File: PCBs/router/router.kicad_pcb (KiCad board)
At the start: 2 copper layers, 77.9 x 90 mm, 0 parts

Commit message: starting to place things
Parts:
- added C1: CP1, Capacitor_THT:CP_Radial_D5.0mm_P2.00mm, F.Cu at (197.1, 58.4)
- added C2: CP1, Capacitor_THT:CP_Radial_D5.0mm_P2.00mm, F.Cu at (202.2, 70.6)
- added C3: C_Small, Capacitor_THT:C_Disc_D5.0mm_W2.5mm_P5.00mm, F.Cu at (133.5, 102.1)
- added C4: C_Small, Capacitor_THT:C_Disc_D5.0mm_W2.5mm_P5.00mm, F.Cu at (133.6, 121.4)
- added C5: C_Small, Capacitor_THT:C_Disc_D4.3mm_W1.9mm_P5.00mm, F.Cu at (148.8, 78.2)
- added C6: C_Small, Capacitor_THT:C_Disc_D5.0mm_W2.5mm_P5.00mm, F.Cu at (157.4, 121.4)
- added C7: C_Small, Capacitor_THT:C_Disc_D5.0mm_W2.5mm_P5.00mm, F.Cu at (157.5, 102.1)
- added C8: C_Small, Capacitor_THT:C_Disc_D4.3mm_W1.9mm_P5.00mm, F.Cu at (172.7, 78.2)
- added D1: LED, LED_THT:LED_D3.0mm, F.Cu at (206.8, 64.5)
- added J1: Conn_01x06_Male, Connector_PinHeader_2.54mm:PinHeader_1x06_P2.54mm_Vertical, F.Cu at (227.6, 88.5)
- added J10: Conn_01x06_Male, Connector_PinHeader_2.54mm:PinHeader_1x06_P2.54mm_Vertical, F.Cu at (148.3, 81.8)
- added J11: Conn_01x06_Male, Connector_PinHeader_2.54mm:PinHeader_1x06_P2.54mm_Vertical, F.Cu at (248.3, 105.8)
- added J12: Conn_01x06_Female, Connector_PinSocket_2.54mm:PinSocket_1x06_P2.54mm_Horizontal, F.Cu at (261.7, 105.8)
- added J13: Conn_01x06_Male, Connector_PinHeader_2.54mm:PinHeader_1x06_P2.54mm_Vertical, F.Cu at (262.2, 88.5)
- added J14: Conn_01x06_Female, Connector_PinSocket_2.54mm:PinSocket_1x06_P2.54mm_Horizontal, F.Cu at (289.0, 88.5)
- added J15: Conn_01x06_Male, Connector_PinHeader_2.54mm:PinHeader_1x06_P2.54mm_Vertical, F.Cu at (172.2, 81.8)
- added J2: Conn_01x06_Male, Connector_PinHeader_2.54mm:PinHeader_1x06_P2.54mm_Horizontal, F.Cu at (230.2, 123.2)
- added J3: Conn_01x06_Male, Connector_PinHeader_2.54mm:PinHeader_1x06_P2.54mm_Vertical, F.Cu at (243.6, 105.8)
- added J4: Conn_01x06_Male, Connector_PinHeader_2.54mm:PinHeader_1x06_P2.54mm_Horizontal, F.Cu at (230.2, 105.8)
- added J5: Conn_01x06_Male, Connector_PinHeader_2.54mm:PinHeader_1x06_P2.54mm_Vertical, F.Cu at (252.9, 88.5)
- added J6: Conn_01x06_Male, Connector_PinHeader_2.54mm:PinHeader_1x06_P2.54mm_Horizontal, F.Cu at (239.5, 88.5)
- added J7: Conn_01x04_Male, Connector_PinHeader_2.54mm:PinHeader_1x04_P2.54mm_Vertical, F.Cu at (222.8, 125.8)
- added J8: Conn_01x06_Male, Connector_PinHeader_2.54mm:PinHeader_1x06_P2.54mm_Vertical, F.Cu at (234.9, 88.5)
- added J9: Conn_01x06_Female, Connector_PinSocket_2.54mm:PinSocket_1x06_P2.54mm_Horizontal, F.Cu at (275.6, 88.5)
- added R1: R, Resistor_THT:R_Axial_DIN0207_L6.3mm_D2.5mm_P7.62mm_Horizontal, F.Cu at (134.1, 85.9)
- added R2: R, Resistor_THT:R_Axial_DIN0207_L6.3mm_D2.5mm_P7.62mm_Horizontal, F.Cu at (210.3, 59.4)
- added R3: R, Resistor_THT:R_Axial_DIN0207_L6.3mm_D2.5mm_P7.62mm_Horizontal, F.Cu at (158.0, 85.9)
- added SW1: SW_MEC_5E, Button_Switch_THT:SW_TH_Tactile_Omron_B3F-10xx, F.Cu at (137.2, 81.3)
- added SW2: SW_MEC_5E, Button_Switch_THT:SW_TH_Tactile_Omron_B3F-10xx, F.Cu at (161.0, 81.3)
- added U1: LM7805_TO220, Package_TO_SOT_THT:TO-220-3_Vertical, F.Cu at (197.1, 65.5)
- added U2: ATmega328P-PU, Package_DIP:DIP-28_W7.62mm_Socket, F.Cu at (136.7, 88.9)
- added U3: ATmega328P-PU, Package_DIP:DIP-28_W7.62mm_Socket, F.Cu at (160.5, 88.9)
- added Y1: Crystal, SamacSys_Parts:HC_49US__AT49_PTH, F.Cu at (130.6, 111.8)
- added Y2: Crystal, SamacSys_Parts:HC_49US__AT49_PTH, F.Cu at (154.4, 111.8)

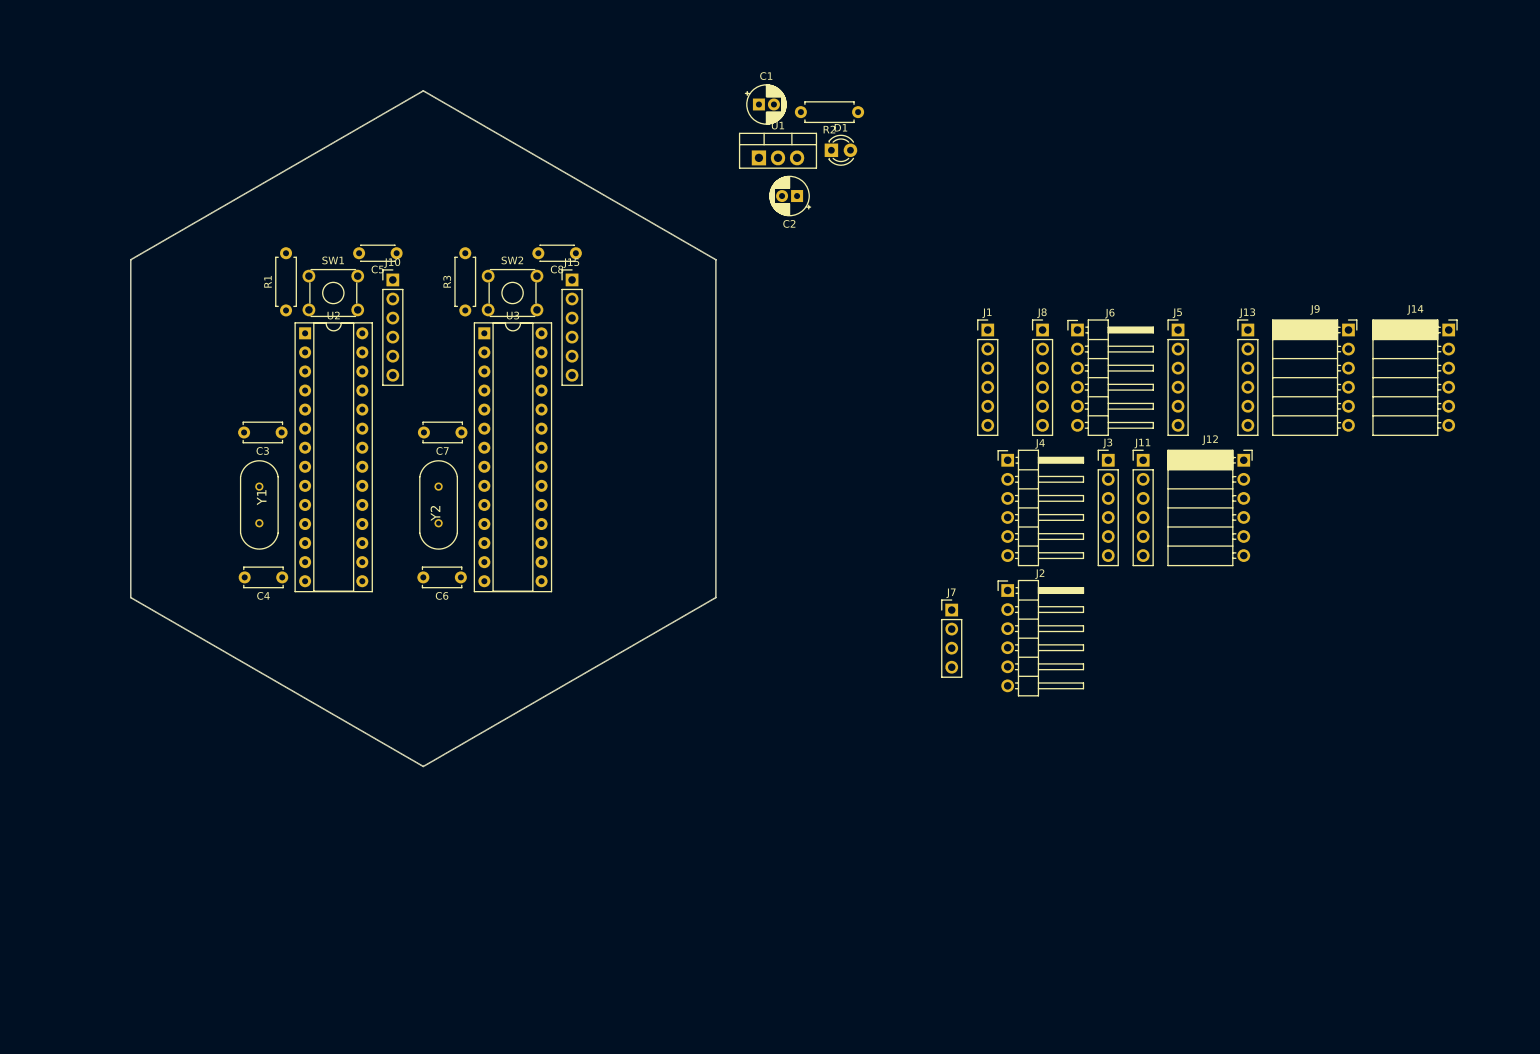
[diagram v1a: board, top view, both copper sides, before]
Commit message: add edges and update footprints
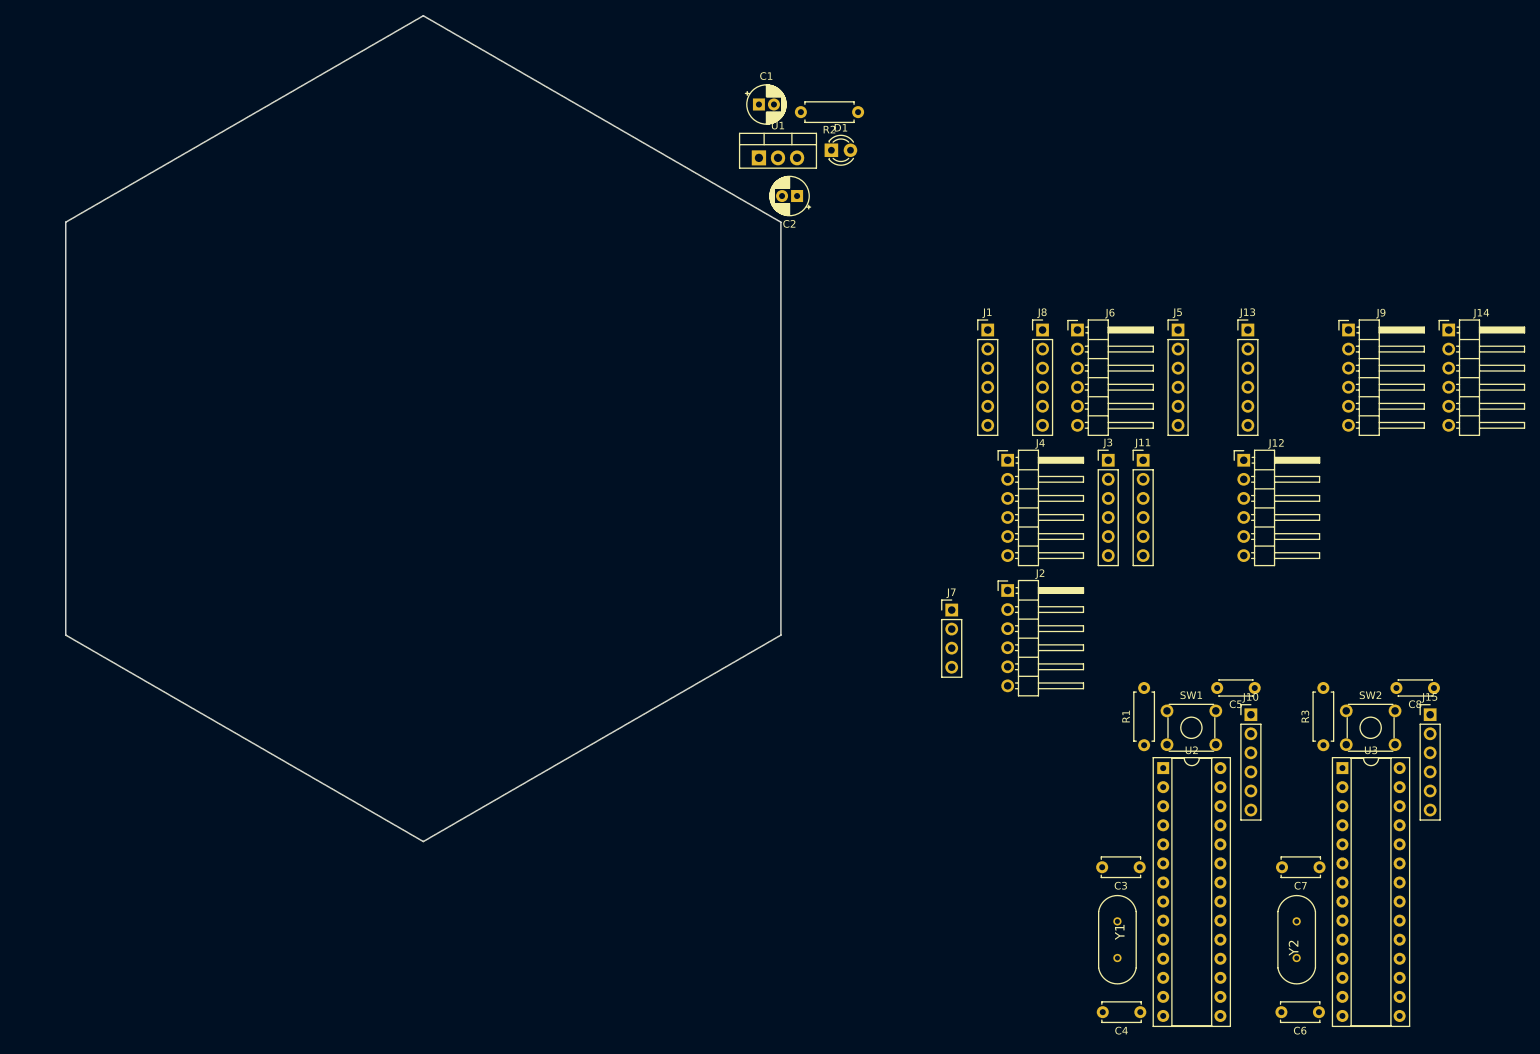
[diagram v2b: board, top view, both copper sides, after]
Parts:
- J12, J14, J9: value Conn_01x06_Female -> Conn_01x06_Male; footprint Connector_PinSocket_2.54mm:PinSocket_1x06_P2.54mm_Horizontal -> Connector_PinHeader_2.54mm:PinHeader_1x06_P2.54mm_Horizontal
- moved Y2 128.1 mm to (268.7, 169.7)
- moved C3 128.1 mm to (247.8, 160.0)
- moved C5 128.1 mm to (263.1, 136.1)
- moved J10 128.1 mm to (262.6, 139.7)
- moved J15 128.1 mm to (286.5, 139.7)
- moved R1 128.1 mm to (248.4, 143.8)
- moved R3 128.1 mm to (272.3, 143.8)
- moved SW1 128.1 mm to (251.5, 139.2)
- moved SW2 128.1 mm to (275.3, 139.2)
- moved U2 128.1 mm to (251.0, 146.8)
- moved C4 128.1 mm to (247.9, 179.3)
- moved C6 128.1 mm to (271.7, 179.3)
- moved C7 128.1 mm to (271.8, 160.0)
- moved C8 128.1 mm to (287.0, 136.1)
- moved U3 128.1 mm to (274.8, 146.8)
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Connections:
- J12 pad 2: Net-(J11-Pad5) -> Net-(J11-Pad2)
- J12 pad 5: Net-(J11-Pad2) -> Net-(J11-Pad5)
- J14 pad 2: Net-(J13-Pad5) -> Net-(J13-Pad2)
- J14 pad 5: Net-(J13-Pad2) -> Net-(J13-Pad5)
- J9 pad 2: Net-(J8-Pad5) -> Net-(J8-Pad2)
- J9 pad 5: Net-(J8-Pad2) -> Net-(J8-Pad5)
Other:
- board size 77.9 x 90 mm -> 95.3 x 110 mm

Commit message: set connector locations
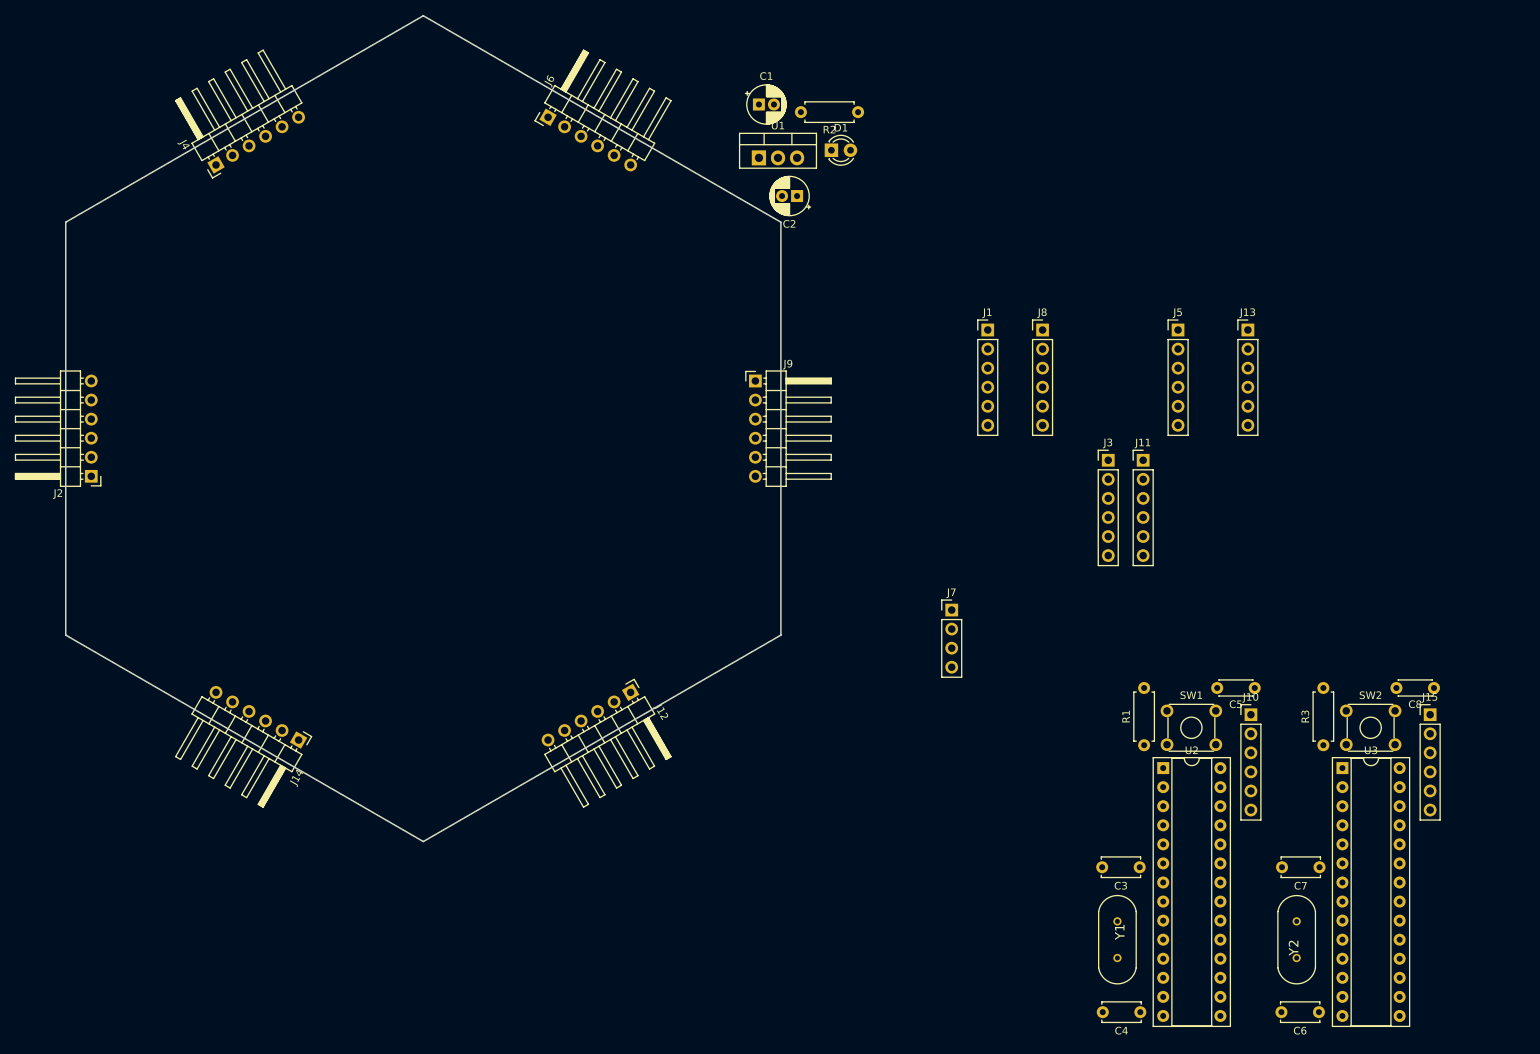
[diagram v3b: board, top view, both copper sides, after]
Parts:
- moved J14 162.6 mm to (135.8, 143.1), turned to 240 degrees
- moved J2 123.0 mm to (108.2, 108.0), turned to 180 degrees
- moved J4 112.5 mm to (124.8, 66.5), turned to 120 degrees
- moved J12 87.3 mm to (180.0, 136.7), turned to 300 degrees
- moved J9 79.3 mm to (196.6, 95.2)
- moved J6 76.0 mm to (169.0, 60.1), turned to 60 degrees

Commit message: place inner ring
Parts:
- moved J13 133.6 mm to (138.4, 138.5), turned to 240 degrees
- moved J3 121.3 mm to (127.4, 71.0), turned to 120 degrees
- moved J1 115.8 mm to (113.4, 108.0), turned to 180 degrees
- moved J5 89.7 mm to (166.4, 64.7), turned to 60 degrees
- moved J11 75.6 mm to (177.4, 132.2), turned to 300 degrees
- moved J8 44.0 mm to (191.4, 95.2)

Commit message: place actor port
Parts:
- moved J7 50.1 mm to (191.8, 86.4), turned to 180 degrees
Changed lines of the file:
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@@
     (add_net "Net-(J10-Pad2)")
     (add_net "Net-(J10-Pad3)")
-    (add_net "Net-(J10-Pad5)")
     (add_net "Net-(J11-Pad2)")
     (add_net "Net-(J11-Pad5)")
@@
     (add_net "Net-(J15-Pad2)")
     (add_net "Net-(J15-Pad3)")
-    (add_net "Net-(J15-Pad5)")
     (add_net "Net-(J3-Pad2)")
     (add_net "Net-(J3-Pad5)")
@@
     (add_net "Net-(J8-Pad2)")
     (add_net "Net-(J8-Pad5)")
-    (add_net "Net-(SW1-Pad2)")
-    (add_net "Net-(SW1-Pad4)")
-    (add_net "Net-(SW2-Pad2)")
-    (add_net "Net-(SW2-Pad4)")
-    (add_net "Net-(U2-Pad25)")
-    (add_net "Net-(U2-Pad26)")
     (add_net "Net-(U2-Pad27)")
     (add_net "Net-(U2-Pad28)")
-    (add_net "Net-(U3-Pad11)")
-    (add_net "Net-(U3-Pad12)")
-    (add_net "Net-(U3-Pad13)")
-    (add_net "Net-(U3-Pad14)")
-    (add_net "Net-(U3-Pad15)")
-    (add_net "Net-(U3-Pad16)")
-    (add_net "Net-(U3-Pad17)")
-    (add_net "Net-(U3-Pad18)")
-    (add_net "Net-(U3-Pad19)")
-    (add_net "Net-(U3-Pad23)")
-    (add_net "Net-(U3-Pad24)")
-    (add_net "Net-(U3-Pad25)")
-    (add_net "Net-(U3-Pad26)")
-    (add_net "Net-(U3-Pad4)")
-    (add_net "Net-(U3-Pad5)")
-    (add_net "Net-(U3-Pad6)")
   )
   (module Connector_PinHeader_2.54mm:PinHeader_1x06_P2.54mm_Horizontal (layer F.Cu)
@@
       (effects (font (size 1 1) (thickness 0.15)))
     )
-    (fp_text user %R (at 2.77 6.35 90) (layer F.Fab)
-      (effects (font (size 1 1) (thickness 0.15)))
-    )
     (fp_line (start 2.135 -1.27) (end 4.04 -1.27) (layer F.Fab) (width 0.1))
     (fp_line (start 4.04 -1.27) (end 4.04 13.97) (layer F.Fab) (width 0.1))
@@
     (fp_line (start 10.55 14.5) (end 10.55 -1.8) (layer F.CrtYd) (width 0.05))
     (fp_line (start 10.55 -1.8) (end -1.8 -1.8) (layer F.CrtYd) (width 0.05))
+    (fp_text user %R (at 2.77 6.35 90) (layer F.Fab)
+      (effects (font (size 1 1) (thickness 0.15)))
+    )
     (pad 6 thru_hole oval (at 0 12.7) (size 1.7 1.7) (drill 1) (layers *.Cu *.Mask)
       (net 2 +9V))
@@
   )
   (module Connector_PinHeader_2.54mm:PinHeader_1x04_P2.54mm_Vertical (layer F.Cu)
-    (at 222.784225 125.758)
+    (at 191.77 86.36 180)
     (descr "Through hole straight pin header, 1x04, 2.54mm pitch, single row")
     (tags "Through hole pin header THT 1x04 2.54mm single row")
@@
       (effects (font (size 1 1) (thickness 0.15)))
     )
-    (pad 4 thru_hole oval (at 0 7.62) (size 1.7 1.7) (drill 1) (layers *.Cu *.Mask)
+    (pad 4 thru_hole oval (at 0 7.62 180) (size 1.7 1.7) (drill 1) (layers *.Cu *.Mask)
       (net 2 +9V))
-    (pad 3 thru_hole oval (at 0 5.08) (size 1.7 1.7) (drill 1) (layers *.Cu *.Mask)
+    (pad 3 thru_hole oval (at 0 5.08 180) (size 1.7 1.7) (drill 1) (layers *.Cu *.Mask)
       (net 19 "Net-(J7-Pad3)"))
-    (pad 2 thru_hole oval (at 0 2.54) (size 1.7 1.7) (drill 1) (layers *.Cu *.Mask)
+    (pad 2 thru_hole oval (at 0 2.54 180) (size 1.7 1.7) (drill 1) (layers *.Cu *.Mask)
       (net 20 "Net-(J7-Pad2)"))
-    (pad 1 thru_hole rect (at 0 0) (size 1.7 1.7) (drill 1) (layers *.Cu *.Mask)
+    (pad 1 thru_hole rect (at 0 0 180) (size 1.7 1.7) (drill 1) (layers *.Cu *.Mask)
       (net 1 GND))
     (model ${KISYS3DMOD}/Connector_PinHeader_2.54mm.3dshapes/PinHeader_1x04_P2.54mm_Vertical.wrl

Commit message: and holes for router
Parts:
- added H1: MountingHole, MountingHole:MountingHole_3.2mm_M3, F.Cu at (152.4, 67.6)
- added H2: MountingHole, MountingHole:MountingHole_3.2mm_M3, F.Cu at (196.6, 127.1)
- added H3: MountingHole, MountingHole:MountingHole_3.2mm_M3, F.Cu at (108.2, 127.1)
